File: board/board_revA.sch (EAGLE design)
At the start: 64 parts, among them Q2 ULN2003AD, Y1 8Mhz

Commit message: [Board Rev A] Tweaking resistor values
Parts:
- R13: value 1K -> 2.2K
- R30, R32, R4, R6, R7: value 10K -> 470K 0.1%
- R31: value 1K -> 470K 0.1%
- R5: value 10K -> 100K
- R8: value 47K -> 470K 0.1%
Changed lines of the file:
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@@
 <part name="+3V19" library="supply1" deviceset="+3V3" device=""/>
 <part name="GND35" library="supply1" deviceset="GND" device=""/>
-<part name="R30" library="SparkFun-Resistors" deviceset="RESISTOR" device="0603-RES" value="10K"/>
-<part name="R31" library="SparkFun-Resistors" deviceset="RESISTOR" device="0603-RES" value="1K"/>
+<part name="R30" library="SparkFun-Resistors" deviceset="RESISTOR" device="0603-RES" value="470K 0.1%"/>
+<part name="R31" library="SparkFun-Resistors" deviceset="RESISTOR" device="0603-RES" value="470K 0.1%"/>
 <part name="GND34" library="supply1" deviceset="GND" device=""/>
 <part name="P+10" library="supply1" deviceset="VCC" device=""/>
-<part name="R32" library="SparkFun-Resistors" deviceset="RESISTOR" device="0603-RES" value="10K"/>
+<part name="R32" library="SparkFun-Resistors" deviceset="RESISTOR" device="0603-RES" value="470K 0.1%"/>
 <part name="C34" library="SparkFun-Passives" deviceset="CAP" device="0603-CAP" value="4.7uF"/>
 <part name="S1" library="SparkFun-Electromechanical" deviceset="SWITCH-SPDT" device="PTH"/>
@@
 <part name="P+3" library="supply1" deviceset="+12V" device=""/>
 <part name="GND5" library="supply1" deviceset="GND" device=""/>
-<part name="R4" library="SparkFun-Resistors" deviceset="RESISTOR" device="0603-RES" value="10K"/>
-<part name="R6" library="SparkFun-Resistors" deviceset="RESISTOR" device="0603-RES" value="10K"/>
-<part name="R7" library="SparkFun-Resistors" deviceset="RESISTOR" device="0603-RES" value="10K"/>
+<part name="R4" library="SparkFun-Resistors" deviceset="RESISTOR" device="0603-RES" value="470K 0.1%"/>
+<part name="R6" library="SparkFun-Resistors" deviceset="RESISTOR" device="0603-RES" value="470K 0.1%"/>
+<part name="R7" library="SparkFun-Resistors" deviceset="RESISTOR" device="0603-RES" value="470K 0.1%"/>
 <part name="GND6" library="supply1" deviceset="GND" device=""/>
 <part name="GND8" library="supply1" deviceset="GND" device=""/>
@@
 <part name="CON_AN" library="SparkFun-Connectors" deviceset="M03" device="PTH"/>
 <part name="GND15" library="supply1" deviceset="GND" device=""/>
-<part name="R5" library="SparkFun-Resistors" deviceset="RESISTOR" device="0603-RES" value="10K"/>
+<part name="R5" library="SparkFun-Resistors" deviceset="RESISTOR" device="0603-RES" value="100K"/>
 <part name="C4" library="SparkFun-Capacitors" deviceset="CAP" device="0603-CAP" value="100nF"/>
-<part name="R8" library="SparkFun-Resistors" deviceset="RESISTOR" device="0603-RES" value="47K"/>
+<part name="R8" library="SparkFun-Resistors" deviceset="RESISTOR" device="0603-RES" value="470K 0.1%"/>
 <part name="D7" library="diode" deviceset="BAT54S" device=""/>
 <part name="+3V10" library="supply1" deviceset="+3V3" device=""/>
@@
 <part name="+3V11" library="supply1" deviceset="+3V3" device=""/>
 <part name="IC_KLINE" library="misc" deviceset="MCP2004" device=""/>
-<part name="R13" library="SparkFun-Resistors" deviceset="RESISTOR" device="0603-RES" value="1K"/>
+<part name="R13" library="SparkFun-Resistors" deviceset="RESISTOR" device="0603-RES" value="2.2K"/>
 <part name="D6" library="SparkFun-DiscreteSemi" deviceset="DIODE" device="SMA" value="B240A"/>
 <part name="Y1" library="SparkFun-FreqCtrl" deviceset="CRYSTAL" device="HC49US" value="8Mhz"/>
@@
 <instance part="+3V19" gate="G$1" x="110.49" y="124.46" rot="MR0"/>
 <instance part="GND35" gate="1" x="110.49" y="104.14"/>
-<instance part="R30" gate="G$1" x="62.23" y="156.21" rot="R90"/>
-<instance part="R31" gate="G$1" x="62.23" y="146.05" rot="R90"/>
+<instance part="R30" gate="G$1" x="62.23" y="156.21" smashed="yes" rot="R90">
+<attribute name="NAME" x="60.7314" y="152.4" size="1.778" layer="95" rot="R90"/>
+<attribute name="VALUE" x="65.532" y="152.4" size="1.778" layer="96" rot="R90"/>
+</instance>
+<instance part="R31" gate="G$1" x="62.23" y="146.05" smashed="yes" rot="R90">
+<attribute name="NAME" x="60.7314" y="142.24" size="1.778" layer="95" rot="R90"/>
+<attribute name="VALUE" x="65.532" y="138.43" size="1.778" layer="96" rot="R90"/>
+</instance>
 <instance part="GND34" gate="1" x="62.23" y="138.43"/>
 <instance part="P+10" gate="VCC" x="62.23" y="163.83"/>
-<instance part="R32" gate="G$1" x="36.83" y="120.65"/>
+<instance part="R32" gate="G$1" x="36.83" y="120.65" smashed="yes">
+<attribute name="NAME" x="33.02" y="122.1486" size="1.778" layer="95"/>
+<attribute name="VALUE" x="19.05" y="119.888" size="1.778" layer="96"/>
+</instance>
 <instance part="C34" gate="G$1" x="74.93" y="17.78"/>
 <instance part="S1" gate="1" x="77.47" y="59.69"/>
@@
 <instance part="GND5" gate="1" x="31.75" y="96.52"/>
 <instance part="R4" gate="G$1" x="38.1" y="109.22"/>
-<instance part="R6" gate="G$1" x="48.26" y="115.57" rot="R90"/>
+<instance part="R6" gate="G$1" x="48.26" y="115.57" smashed="yes" rot="R90">
+<attribute name="NAME" x="46.7614" y="111.76" size="1.778" layer="95" rot="R90"/>
+<attribute name="VALUE" x="51.562" y="110.49" size="1.778" layer="96" rot="R90"/>
+</instance>
 <instance part="R7" gate="G$1" x="59.69" y="104.14" rot="R90"/>
 <instance part="GND6" gate="1" x="346.71" y="53.34"/>
@@
 <instance part="CON_AN" gate="G$1" x="24.13" y="106.68"/>
 <instance part="GND15" gate="1" x="43.18" y="78.74"/>
-<instance part="R5" gate="G$1" x="88.9" y="80.01" rot="R180"/>
+<instance part="R5" gate="G$1" x="88.9" y="80.01" smashed="yes" rot="R180">
+<attribute name="NAME" x="92.71" y="78.5114" size="1.778" layer="95" rot="R180"/>
+<attribute name="VALUE" x="88.9" y="78.232" size="1.778" layer="96" rot="R180"/>
+</instance>
 <instance part="C4" gate="G$1" x="53.34" y="88.9" rot="R90"/>
-<instance part="R8" gate="G$1" x="60.96" y="88.9" rot="R180"/>
-<instance part="D7" gate="G$1" x="44.45" y="120.65" rot="R90"/>
+<instance part="R8" gate="G$1" x="60.96" y="88.9" smashed="yes" rot="R180">
+<attribute name="NAME" x="64.77" y="87.4014" size="1.778" layer="95" rot="R180"/>
+<attribute name="VALUE" x="69.85" y="92.202" size="1.778" layer="96" rot="R180"/>
+</instance>
+<instance part="D7" gate="G$1" x="44.45" y="120.65" smashed="yes" rot="R90">
+<attribute name="NAME" x="47.5234" y="121.412" size="1.778" layer="95" rot="R90"/>
+<attribute name="VALUE" x="43.3324" y="113.792" size="1.778" layer="96" rot="R90"/>
+</instance>
 <instance part="+3V10" gate="G$1" x="44.45" y="130.81" rot="MR0"/>
-<instance part="D3" gate="G$1" x="54.61" y="109.22" rot="R90"/>
-<instance part="+3V9" gate="G$1" x="54.61" y="118.11" rot="MR0"/>
+<instance part="D3" gate="G$1" x="54.61" y="109.22" smashed="yes" rot="R90">
+<attribute name="NAME" x="52.6034" y="103.632" size="1.778" layer="95" rot="R90"/>
+<attribute name="VALUE" x="58.5724" y="104.902" size="1.778" layer="96" rot="R90"/>
+</instance>
+<instance part="+3V9" gate="G$1" x="54.61" y="118.11" smashed="yes" rot="MR0">
+<attribute name="VALUE" x="54.61" y="118.11" size="1.778" layer="96" rot="MR90"/>
+</instance>
 <instance part="D4" gate="G$1" x="71.12" y="77.47"/>
 <instance part="+3V8" gate="G$1" x="78.74" y="80.01" rot="MR0"/>

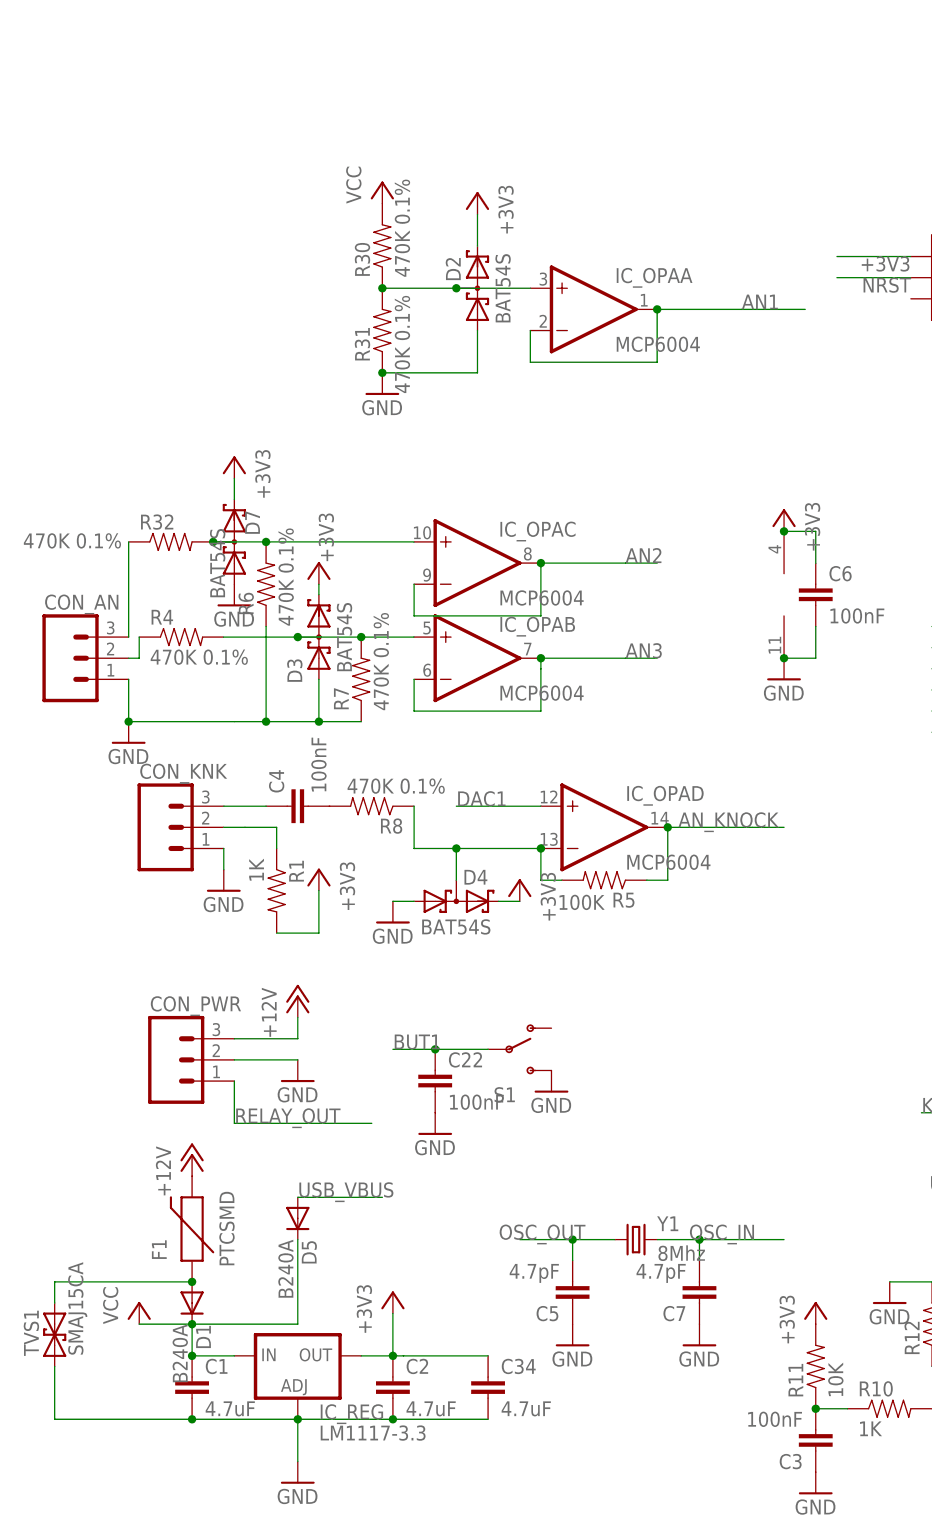
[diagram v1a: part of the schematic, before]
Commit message: [Board Rev A] Tweaking capacitor values
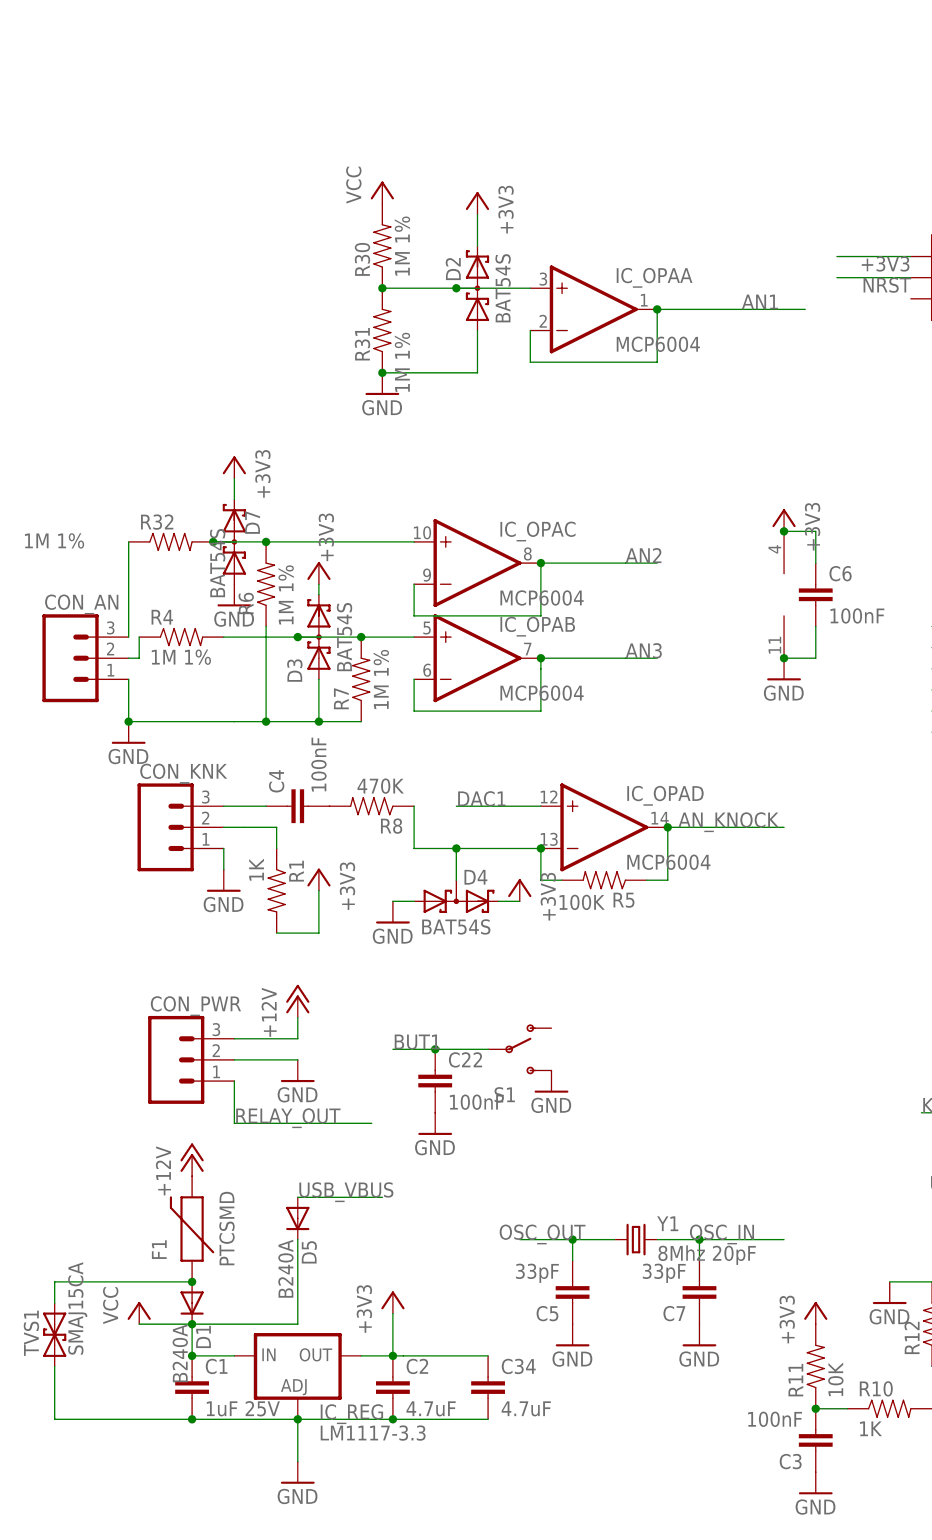
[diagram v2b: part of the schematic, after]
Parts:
- C1: value 4.7uF -> 1uF 25V
- C5, C7: value 4.7pF -> 33pF
- R30, R31, R32, R4, R6, R7: value 470K 0.1% -> 1M 1%
- R8: value 470K 0.1% -> 470K
- Y1: value 8Mhz -> 8Mhz 20pF
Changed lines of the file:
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@@
 <part name="GND1" library="supply1" deviceset="GND" device=""/>
 <part name="+3V1" library="supply1" deviceset="+3V3" device=""/>
-<part name="C1" library="SparkFun-Passives" deviceset="CAP" device="0603-CAP" value="4.7uF"/>
+<part name="C1" library="SparkFun-Passives" deviceset="CAP" device="0603-CAP" value="1uF 25V"/>
 <part name="C2" library="SparkFun-Passives" deviceset="CAP" device="0603-CAP" value="4.7uF"/>
 <part name="P+2" library="supply1" deviceset="+12V" device=""/>
@@
 <part name="+3V19" library="supply1" deviceset="+3V3" device=""/>
 <part name="GND35" library="supply1" deviceset="GND" device=""/>
-<part name="R30" library="SparkFun-Resistors" deviceset="RESISTOR" device="0603-RES" value="470K 0.1%"/>
-<part name="R31" library="SparkFun-Resistors" deviceset="RESISTOR" device="0603-RES" value="470K 0.1%"/>
+<part name="R30" library="SparkFun-Resistors" deviceset="RESISTOR" device="0603-RES" value="1M 1%"/>
+<part name="R31" library="SparkFun-Resistors" deviceset="RESISTOR" device="0603-RES" value="1M 1%"/>
 <part name="GND34" library="supply1" deviceset="GND" device=""/>
 <part name="P+10" library="supply1" deviceset="VCC" device=""/>
-<part name="R32" library="SparkFun-Resistors" deviceset="RESISTOR" device="0603-RES" value="470K 0.1%"/>
+<part name="R32" library="SparkFun-Resistors" deviceset="RESISTOR" device="0603-RES" value="1M 1%"/>
 <part name="C34" library="SparkFun-Passives" deviceset="CAP" device="0603-CAP" value="4.7uF"/>
 <part name="S1" library="SparkFun-Electromechanical" deviceset="SWITCH-SPDT" device="PTH"/>
@@
 <part name="P+3" library="supply1" deviceset="+12V" device=""/>
 <part name="GND5" library="supply1" deviceset="GND" device=""/>
-<part name="R4" library="SparkFun-Resistors" deviceset="RESISTOR" device="0603-RES" value="470K 0.1%"/>
-<part name="R6" library="SparkFun-Resistors" deviceset="RESISTOR" device="0603-RES" value="470K 0.1%"/>
-<part name="R7" library="SparkFun-Resistors" deviceset="RESISTOR" device="0603-RES" value="470K 0.1%"/>
+<part name="R4" library="SparkFun-Resistors" deviceset="RESISTOR" device="0603-RES" value="1M 1%"/>
+<part name="R6" library="SparkFun-Resistors" deviceset="RESISTOR" device="0603-RES" value="1M 1%"/>
+<part name="R7" library="SparkFun-Resistors" deviceset="RESISTOR" device="0603-RES" value="1M 1%"/>
 <part name="GND6" library="supply1" deviceset="GND" device=""/>
 <part name="GND8" library="supply1" deviceset="GND" device=""/>
@@
 <part name="R5" library="SparkFun-Resistors" deviceset="RESISTOR" device="0603-RES" value="100K"/>
 <part name="C4" library="SparkFun-Capacitors" deviceset="CAP" device="0603-CAP" value="100nF"/>
-<part name="R8" library="SparkFun-Resistors" deviceset="RESISTOR" device="0603-RES" value="470K 0.1%"/>
+<part name="R8" library="SparkFun-Resistors" deviceset="RESISTOR" device="0603-RES" value="470K"/>
 <part name="D7" library="diode" deviceset="BAT54S" device=""/>
 <part name="+3V10" library="supply1" deviceset="+3V3" device=""/>
@@
 <part name="R13" library="SparkFun-Resistors" deviceset="RESISTOR" device="0603-RES" value="2.2K"/>
 <part name="D6" library="SparkFun-DiscreteSemi" deviceset="DIODE" device="SMA" value="B240A"/>
-<part name="Y1" library="SparkFun-FreqCtrl" deviceset="CRYSTAL" device="HC49US" value="8Mhz"/>
-<part name="C5" library="SparkFun-Capacitors" deviceset="CAP" device="0603-CAP" value="4.7pF"/>
-<part name="C7" library="SparkFun-Capacitors" deviceset="CAP" device="0603-CAP" value="4.7pF"/>
+<part name="Y1" library="SparkFun-FreqCtrl" deviceset="CRYSTAL" device="HC49US" value="8Mhz 20pF"/>
+<part name="C5" library="SparkFun-Capacitors" deviceset="CAP" device="0603-CAP" value="33pF"/>
+<part name="C7" library="SparkFun-Capacitors" deviceset="CAP" device="0603-CAP" value="33pF"/>
 <part name="GND12" library="supply1" deviceset="GND" device=""/>
 <part name="GND14" library="supply1" deviceset="GND" device=""/>
@@
 <instance part="R8" gate="G$1" x="60.96" y="88.9" smashed="yes" rot="R180">
 <attribute name="NAME" x="64.77" y="87.4014" size="1.778" layer="95" rot="R180"/>
-<attribute name="VALUE" x="69.85" y="92.202" size="1.778" layer="96" rot="R180"/>
+<attribute name="VALUE" x="64.77" y="92.202" size="1.778" layer="96" rot="R180"/>
 </instance>
 <instance part="D7" gate="G$1" x="44.45" y="120.65" smashed="yes" rot="R90">

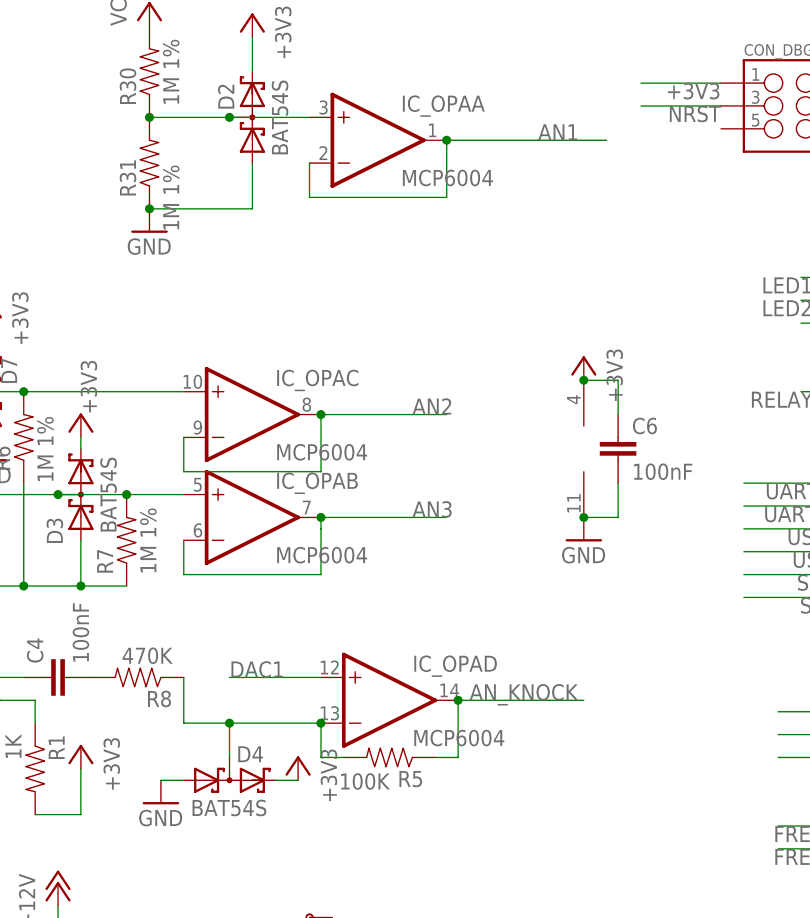
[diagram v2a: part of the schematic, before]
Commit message: [GUI/Code] Rewrote DSP functions, switched to float; Updated DSP library
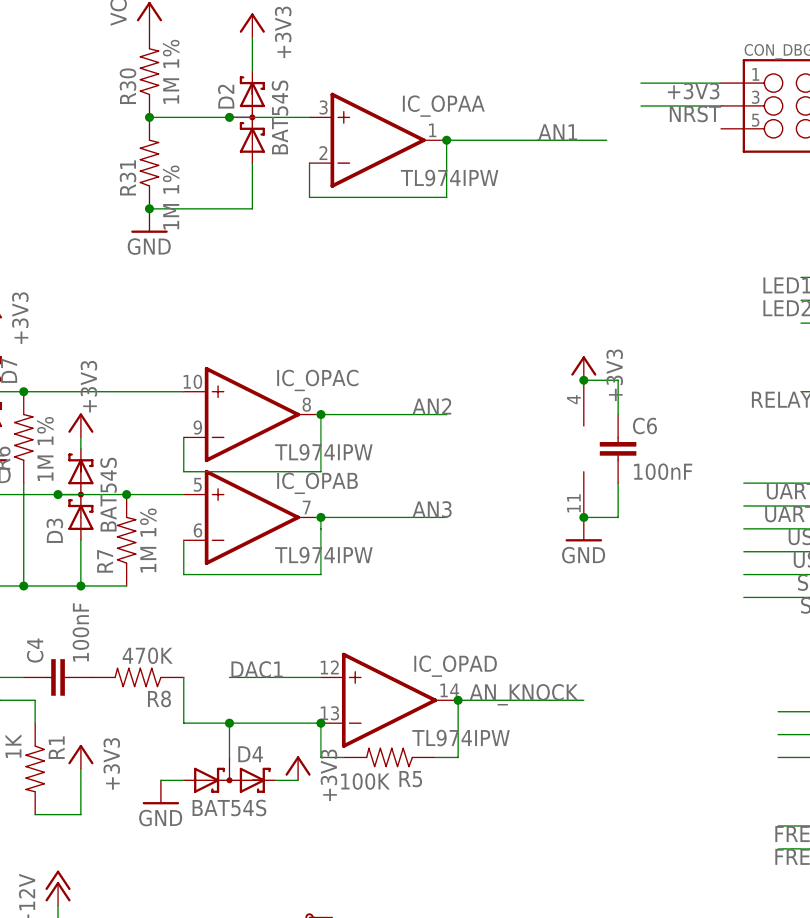
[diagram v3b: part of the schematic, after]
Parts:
- IC_OPA: value MCP6004 -> TL974IPW
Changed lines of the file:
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@@
 <?xml version="1.0" encoding="utf-8"?>
 <!DOCTYPE eagle SYSTEM "eagle.dtd">
-<eagle version="6.5.0">
+<eagle version="7.1.0">
 <drawing>
 <settings>
@@
 <setting verticaltext="up"/>
 </settings>
-<grid distance="0.05" unitdist="inch" unit="inch" style="lines" multiple="1" display="yes" altdistance="0.005" altunitdist="inch" altunit="inch"/>
+<grid distance="0.1" unitdist="inch" unit="inch" style="lines" multiple="1" display="no" altdistance="0.01" altunitdist="inch" altunit="inch"/>
 <layers>
 <layer number="1" name="Top" color="4" fill="1" visible="no" active="no"/>
@@
 <part name="+3V15" library="supply1" deviceset="+3V3" device=""/>
 <part name="CON_DBG" library="SparkFun-Connectors" deviceset="M03X2" device="2X3_SILK_SM"/>
-<part name="IC_OPA" library="linear" deviceset="LMV324?*" device="MZ" value="MCP6004"/>
+<part name="IC_OPA" library="linear" deviceset="LMV324?*" device="MZ" value="TL974IPW"/>
 <part name="+3V19" library="supply1" deviceset="+3V3" device=""/>
 <part name="GND35" library="supply1" deviceset="GND" device=""/>
